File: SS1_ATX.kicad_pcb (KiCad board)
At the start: 4 copper layers, 61.6 x 28.4 mm, 6 parts, among them J1 39299246, J2 15247140, U2 74LVC1G06

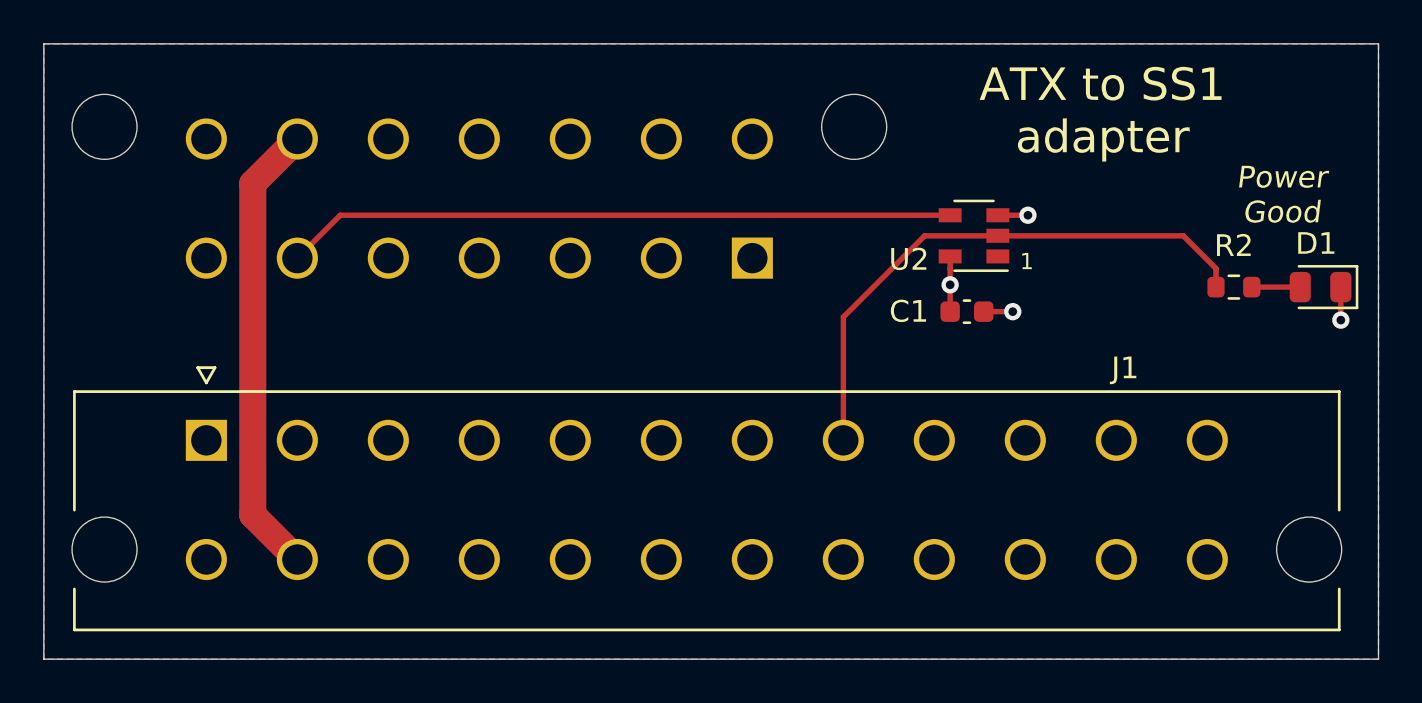
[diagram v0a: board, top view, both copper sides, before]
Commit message: oups, connect ~PS_ON to GND to turn on power
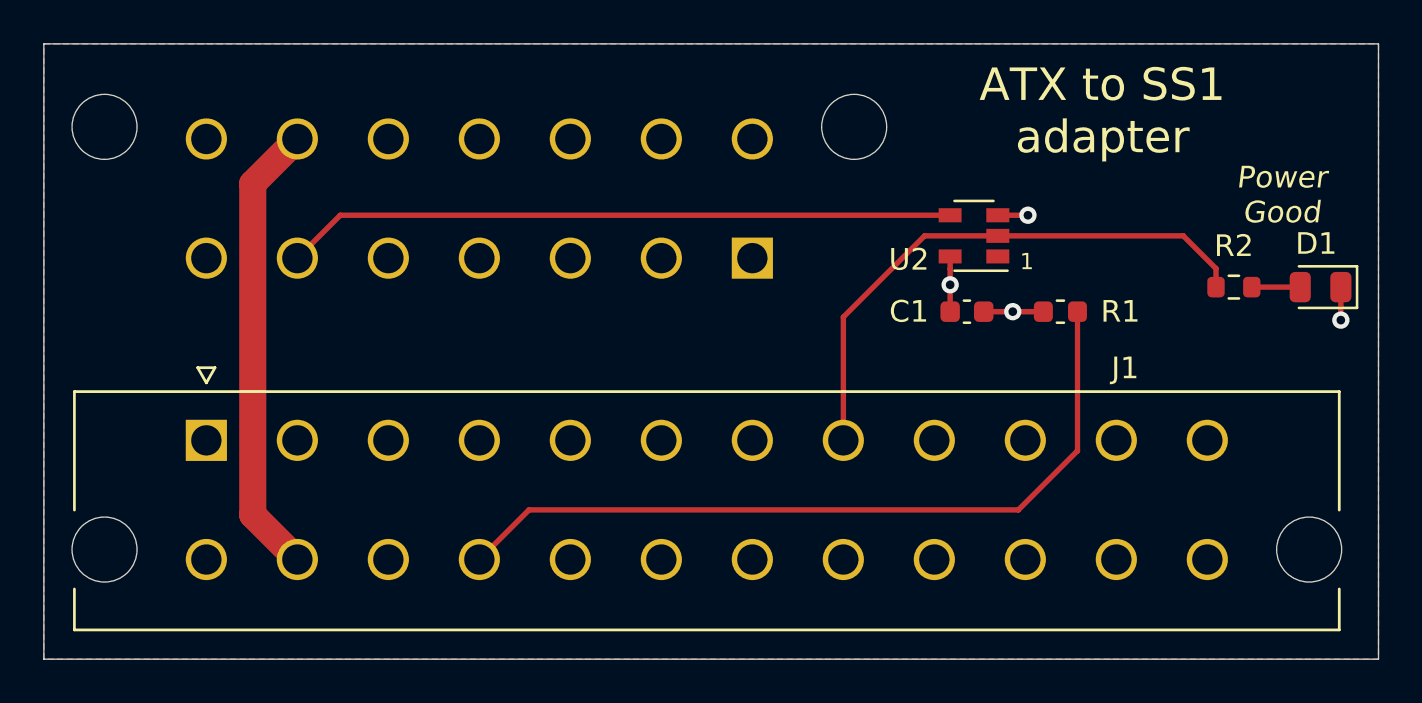
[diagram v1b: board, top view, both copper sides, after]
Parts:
- added R1: 1k, Resistor_SMD:R_0603_1608Metric, F.Cu at (136.9, 122.4)
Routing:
- net ~PS-ON: track 0.00 -> 36.1 mm
- net GND: track 4.25 -> 5.67 mm
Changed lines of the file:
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@@
     (thickness 1.6)
     (drawings 8)
-    (tracks 22)
+    (tracks 27)
     (zones 0)
-    (modules 6)
+    (modules 7)
     (nets 17)
   )
@@
     (add_net PWRONRST)
     (add_net ~PS-ON)
+  )
+  (module Resistor_SMD:R_0603_1608Metric (layer F.Cu)
+    (at 136.92 122.36 180)
+    (descr "Resistor SMD 0603 (1608 Metric), square (rectangular) end terminal, IPC_7351 nominal, (Body size source: http://www.tortai-tech.com/upload/download/2011102023233369053.pdf), generated with kicad-footprint-generator")
+    (tags resistor)
+    (attr smd)
+    (fp_text reference R1 (at -2.77 0 180) (layer F.SilkS)
+      (effects (font (size 1 1) (thickness 0.15)))
+    )
+    (fp_text value 1k (at 0 1.43 180) (layer F.Fab)
+      (effects (font (size 1 1) (thickness 0.15)))
+    )
+    (fp_line (start -0.8 0.4) (end -0.8 -0.4) (layer F.Fab) (width 0.1))
+    (fp_line (start -0.8 -0.4) (end 0.8 -0.4) (layer F.Fab) (width 0.1))
+    (fp_line (start 0.8 -0.4) (end 0.8 0.4) (layer F.Fab) (width 0.1))
+    (fp_line (start 0.8 0.4) (end -0.8 0.4) (layer F.Fab) (width 0.1))
+    (fp_line (start -0.162779 -0.51) (end 0.162779 -0.51) (layer F.SilkS) (width 0.12))
+    (fp_line (start -0.162779 0.51) (end 0.162779 0.51) (layer F.SilkS) (width 0.12))
+    (fp_line (start -1.48 0.73) (end -1.48 -0.73) (layer F.CrtYd) (width 0.05))
+    (fp_line (start -1.48 -0.73) (end 1.48 -0.73) (layer F.CrtYd) (width 0.05))
+    (fp_line (start 1.48 -0.73) (end 1.48 0.73) (layer F.CrtYd) (width 0.05))
+    (fp_line (start 1.48 0.73) (end -1.48 0.73) (layer F.CrtYd) (width 0.05))
+    (fp_text user %R (at 0 0 180) (layer F.Fab)
+      (effects (font (size 0.4 0.4) (thickness 0.06)))
+    )
+    (pad 1 smd roundrect (at -0.7875 0 180) (size 0.875 0.95) (layers F.Cu F.Paste F.Mask) (roundrect_rratio 0.25)
+      (net 3 ~PS-ON))
+    (pad 2 smd roundrect (at 0.7875 0 180) (size 0.875 0.95) (layers F.Cu F.Paste F.Mask) (roundrect_rratio 0.25)
+      (net 1 GND))
+    (model ${KISYS3DMOD}/Resistor_SMD.3dshapes/R_0603_1608Metric.wrl
+      (at (xyz 0 0 0))
+      (scale (xyz 1 1 1))
+      (rotate (xyz 0 0 0))
+    )
   )
   (module MOLEX_15247140 (layer B.Cu)
@@
   (segment (start 149.86328 121.226862) (end 149.86328 122.75) (width 0.25) (layer F.Cu) (net 1))
   (via (at 149.86328 122.75) (size 0.8) (drill 0.4) (layers F.Cu B.Cu) (net 1))
+  (segment (start 136.1325 122.36) (end 134.72 122.36) (width 0.25) (layer F.Cu) (net 1))
   (segment (start 131.83 120.385) (end 131.83 121.12) (width 0.25) (layer F.Cu) (net 2))
   (segment (start 131.83 119.81) (end 131.83 120.385) (width 0.25) (layer F.Cu) (net 2))
   (segment (start 131.83 121.12) (end 131.83 122.36) (width 0.25) (layer F.Cu) (net 2))
   (via (at 131.83 121.12) (size 0.8) (drill 0.4) (layers F.Cu B.Cu) (net 2))
+  (segment (start 137.7075 122.36) (end 137.7075 128.7825) (width 0.25) (layer F.Cu) (net 3))
+  (segment (start 137.7075 128.7825) (end 134.98 131.51) (width 0.25) (layer F.Cu) (net 3))
+  (segment (start 112.39 131.51) (end 110.1 133.8) (width 0.25) (layer F.Cu) (net 3))
+  (segment (start 134.98 131.51) (end 112.39 131.51) (width 0.25) (layer F.Cu) (net 3))
   (segment (start 101.7 133.8) (end 99.64 131.74) (width 1.25) (layer F.Cu) (net 4))
   (segment (start 99.64 131.74) (end 99.64 116.45) (width 1.25) (layer F.Cu) (net 4))

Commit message: upd, notes
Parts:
- R1: value 1k -> 0
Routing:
- net GND: vias 3 -> 7
